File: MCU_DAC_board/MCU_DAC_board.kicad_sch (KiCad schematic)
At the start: 53 parts, among them J11 105-0752-001, J12 Conn_01x03_Pin, J5 54-00127, J6 105-0752-001, J7 Screw_Terminal_01x02, J8 Screw_Terminal_01x02, J9 Conn_02x20_Odd_Even, Q1 FZT953, U1 ADAU1966AWBSTZ

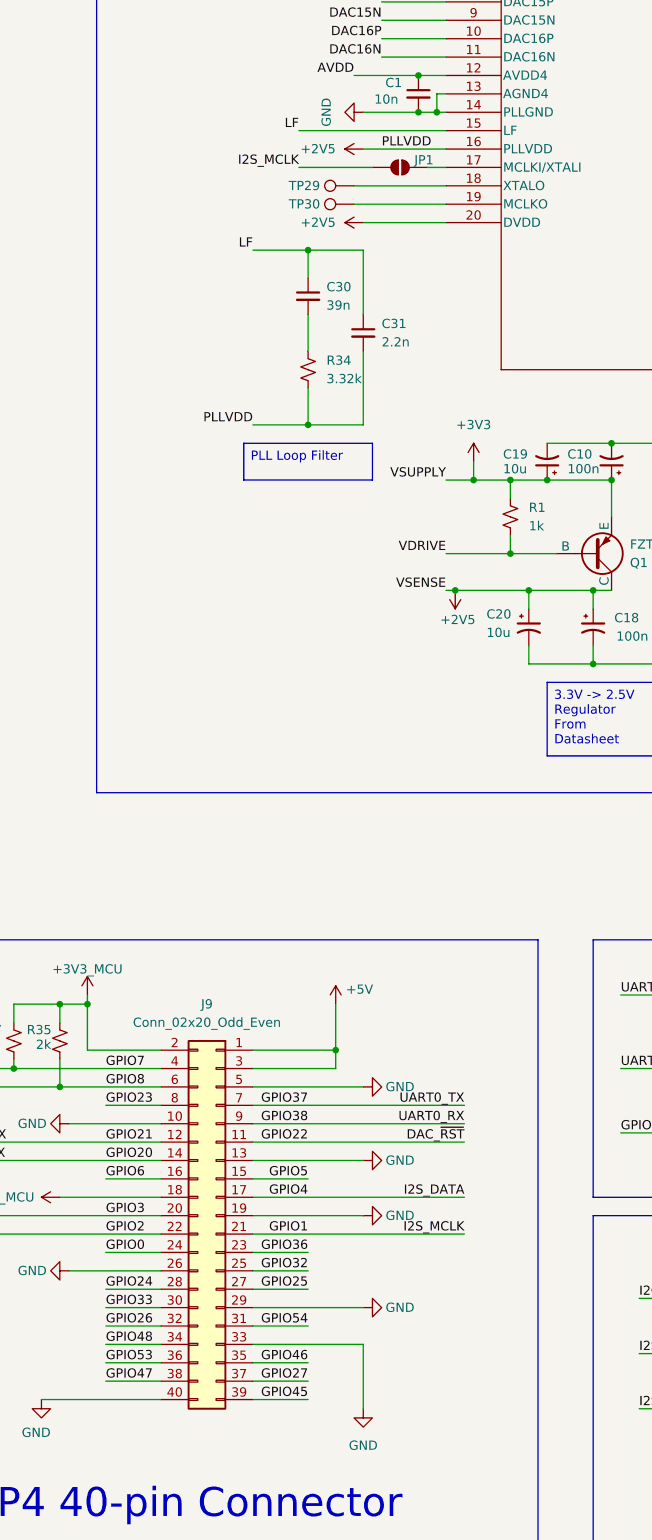
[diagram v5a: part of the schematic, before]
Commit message: Finished MCU to DAC signal routing
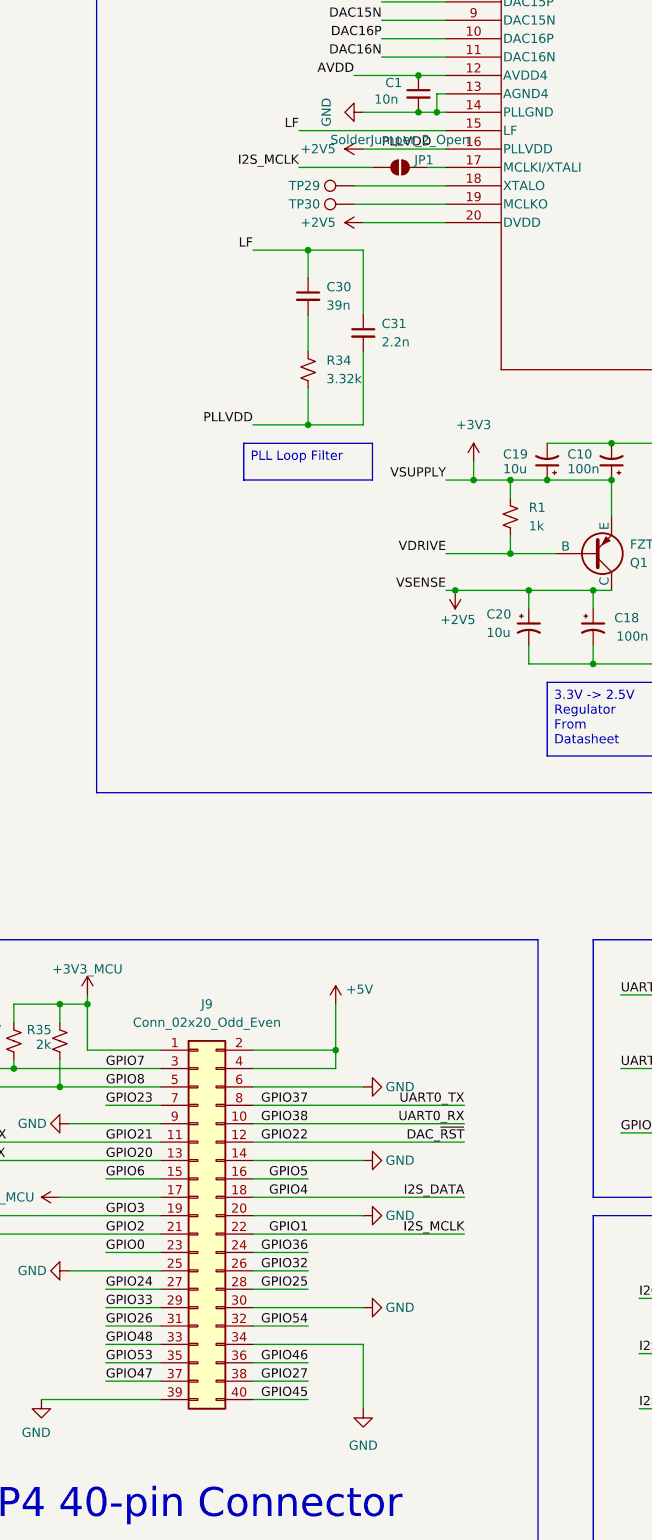
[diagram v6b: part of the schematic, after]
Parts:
- H1, H2, H3, H4: footprint (none) -> MountingHole:MountingHole_2.7mm_M2.5_DIN965_Pad_TopBottom
- JP1: footprint (none) -> Resistor_SMD:R_0201_0603Metric_Pad0.64x0.40mm_HandSolder
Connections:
- net +3V3_MCU: now also J9.1 (Pin_1), J9.17 (Pin_17); no longer J9.18 (Pin_18), J9.2 (Pin_2)
- net +5V: now also J9.2 (Pin_2), J9.4 (Pin_4); no longer J9.1 (Pin_1), J9.3 (Pin_3)
- net DAC_~{RST}: now also J9.12 (Pin_12); no longer J9.11 (Pin_11)
- net GND: now also J9.14 (Pin_14), J9.20 (Pin_20), J9.25 (Pin_25), J9.30 (Pin_30), J9.34 (Pin_34), J9.39 (Pin_39), J9.6 (Pin_6), J9.9 (Pin_9); no longer J9.10 (Pin_10), J9.13 (Pin_13), J9.19 (Pin_19), J9.26 (Pin_26), J9.29 (Pin_29), J9.33 (Pin_33), J9.40 (Pin_40), J9.5 (Pin_5)
- net GPIO0: now also J9.23 (Pin_23); no longer J9.24 (Pin_24)
- net GPIO1: now also J9.22 (Pin_22); no longer J9.21 (Pin_21)
- net GPIO2: now also J9.21 (Pin_21); no longer J9.22 (Pin_22)
- net GPIO20: now also J9.13 (Pin_13); no longer J9.14 (Pin_14)
- net GPIO21: now also J9.11 (Pin_11); no longer J9.12 (Pin_12)
- net GPIO23: now also J9.7 (Pin_7); no longer J9.8 (Pin_8)
- net GPIO24: now also J9.27 (Pin_27); no longer J9.28 (Pin_28)
- net GPIO25: now also J9.28 (Pin_28); no longer J9.27 (Pin_27)
- net GPIO26: now also J9.31 (Pin_31); no longer J9.32 (Pin_32)
- net GPIO27: now also J9.38 (Pin_38); no longer J9.37 (Pin_37)
- net GPIO3: now also J9.19 (Pin_19); no longer J9.20 (Pin_20)
- net GPIO32: now also J9.26 (Pin_26); no longer J9.25 (Pin_25)
- net GPIO33: now also J9.29 (Pin_29); no longer J9.30 (Pin_30)
- net GPIO36: now also J9.24 (Pin_24); no longer J9.23 (Pin_23)
- net GPIO37: now also J9.8 (Pin_8); no longer J9.7 (Pin_7)
- net GPIO38: now also J9.10 (Pin_10); no longer J9.9 (Pin_9)
- net GPIO4: now also J9.18 (Pin_18); no longer J9.17 (Pin_17)
- net GPIO45: now also J9.40 (Pin_40); no longer J9.39 (Pin_39)
- net GPIO46: now also J9.36 (Pin_36); no longer J9.35 (Pin_35)
- net GPIO47: now also J9.37 (Pin_37); no longer J9.38 (Pin_38)
- net GPIO48: now also J9.33 (Pin_33); no longer J9.34 (Pin_34)
- net GPIO5: now also J9.16 (Pin_16); no longer J9.15 (Pin_15)
- net GPIO53: now also J9.35 (Pin_35); no longer J9.36 (Pin_36)
- net GPIO54: now also J9.32 (Pin_32); no longer J9.31 (Pin_31)
- net GPIO6: now also J9.15 (Pin_15); no longer J9.16 (Pin_16)
- net GPIO7: now also J9.3 (Pin_3); no longer J9.4 (Pin_4)
- net GPIO8: now also J9.5 (Pin_5); no longer J9.6 (Pin_6)
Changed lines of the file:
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@@
 		)
 	)
-	(label "GPIO3"
-		(at 207.01 355.6 0)
-		(effects
-			(font
-				(size 1.27 1.27)
-			)
-			(justify left bottom)
-		)
-	)
 	(label "GPIO47"
 		(at 207.01 378.46 0)
@@
 		)
 	)
+	(label "GPIO3"
+		(at 207.01 355.6 0)
+		(effects
+			(font
+				(size 1.27 1.27)
+			)
+			(justify left bottom)
+		)
+	)
 	(label "AVDD"
 		(at 233.68 175.26 180)
@@
 			)
 		)
-		(property "Footprint" ""
+		(property "Footprint" "MountingHole:MountingHole_2.7mm_M2.5_DIN965_Pad_TopBottom"
 			(at 165.1 107.95 0)
 			(effects
@@
 			)
 		)
-		(property "Footprint" ""
+		(property "Footprint" "MountingHole:MountingHole_2.7mm_M2.5_DIN965_Pad_TopBottom"
 			(at 135.89 107.95 0)
 			(effects
@@
 			)
 		)
-		(property "Footprint" ""
+		(property "Footprint" "MountingHole:MountingHole_2.7mm_M2.5_DIN965_Pad_TopBottom"
 			(at 135.89 92.71 0)
 			(effects
@@
 			)
 		)
-		(property "Footprint" ""
+		(property "Footprint" "MountingHole:MountingHole_2.7mm_M2.5_DIN965_Pad_TopBottom"
 			(at 165.1 92.71 0)
 			(effects
@@
 					(size 1.27 1.27)
 				)
-				(hide yes)
 			)
 		)
-		(property "Footprint" ""
+		(property "Footprint" "Resistor_SMD:R_0201_0603Metric_Pad0.64x0.40mm_HandSolder"
 			(at 247.65 210.82 0)
 			(effects
@@
 	(symbol
 		(lib_id "Connector_Generic:Conn_02x20_Odd_Even")
-		(at 222.25 355.6 0)
-		(mirror y)
+		(at 219.71 355.6 0)
 		(unit 1)
 		(exclude_from_sim no)
@@
 		)
 		(property "Footprint" "Connector_PinSocket_2.54mm:PinSocket_2x20_P2.54mm_Vertical_SMD"
-			(at 222.25 355.6 0)
+			(at 219.71 355.6 0)
 			(effects
 				(font
@@
 		)
 		(property "Datasheet" "~"
-			(at 222.25 355.6 0)
+			(at 219.71 355.6 0)
 			(effects
 				(font
@@
 		)
 		(property "Description" "Generic connector, double row, 02x20, odd/even pin numbering scheme (row 1 odd numbers, row 2 even numbers), script generated (kicad-library-utils/schlib/autogen/connector/)"
-			(at 222.25 355.6 0)
+			(at 219.71 355.6 0)
 			(effects
 				(font

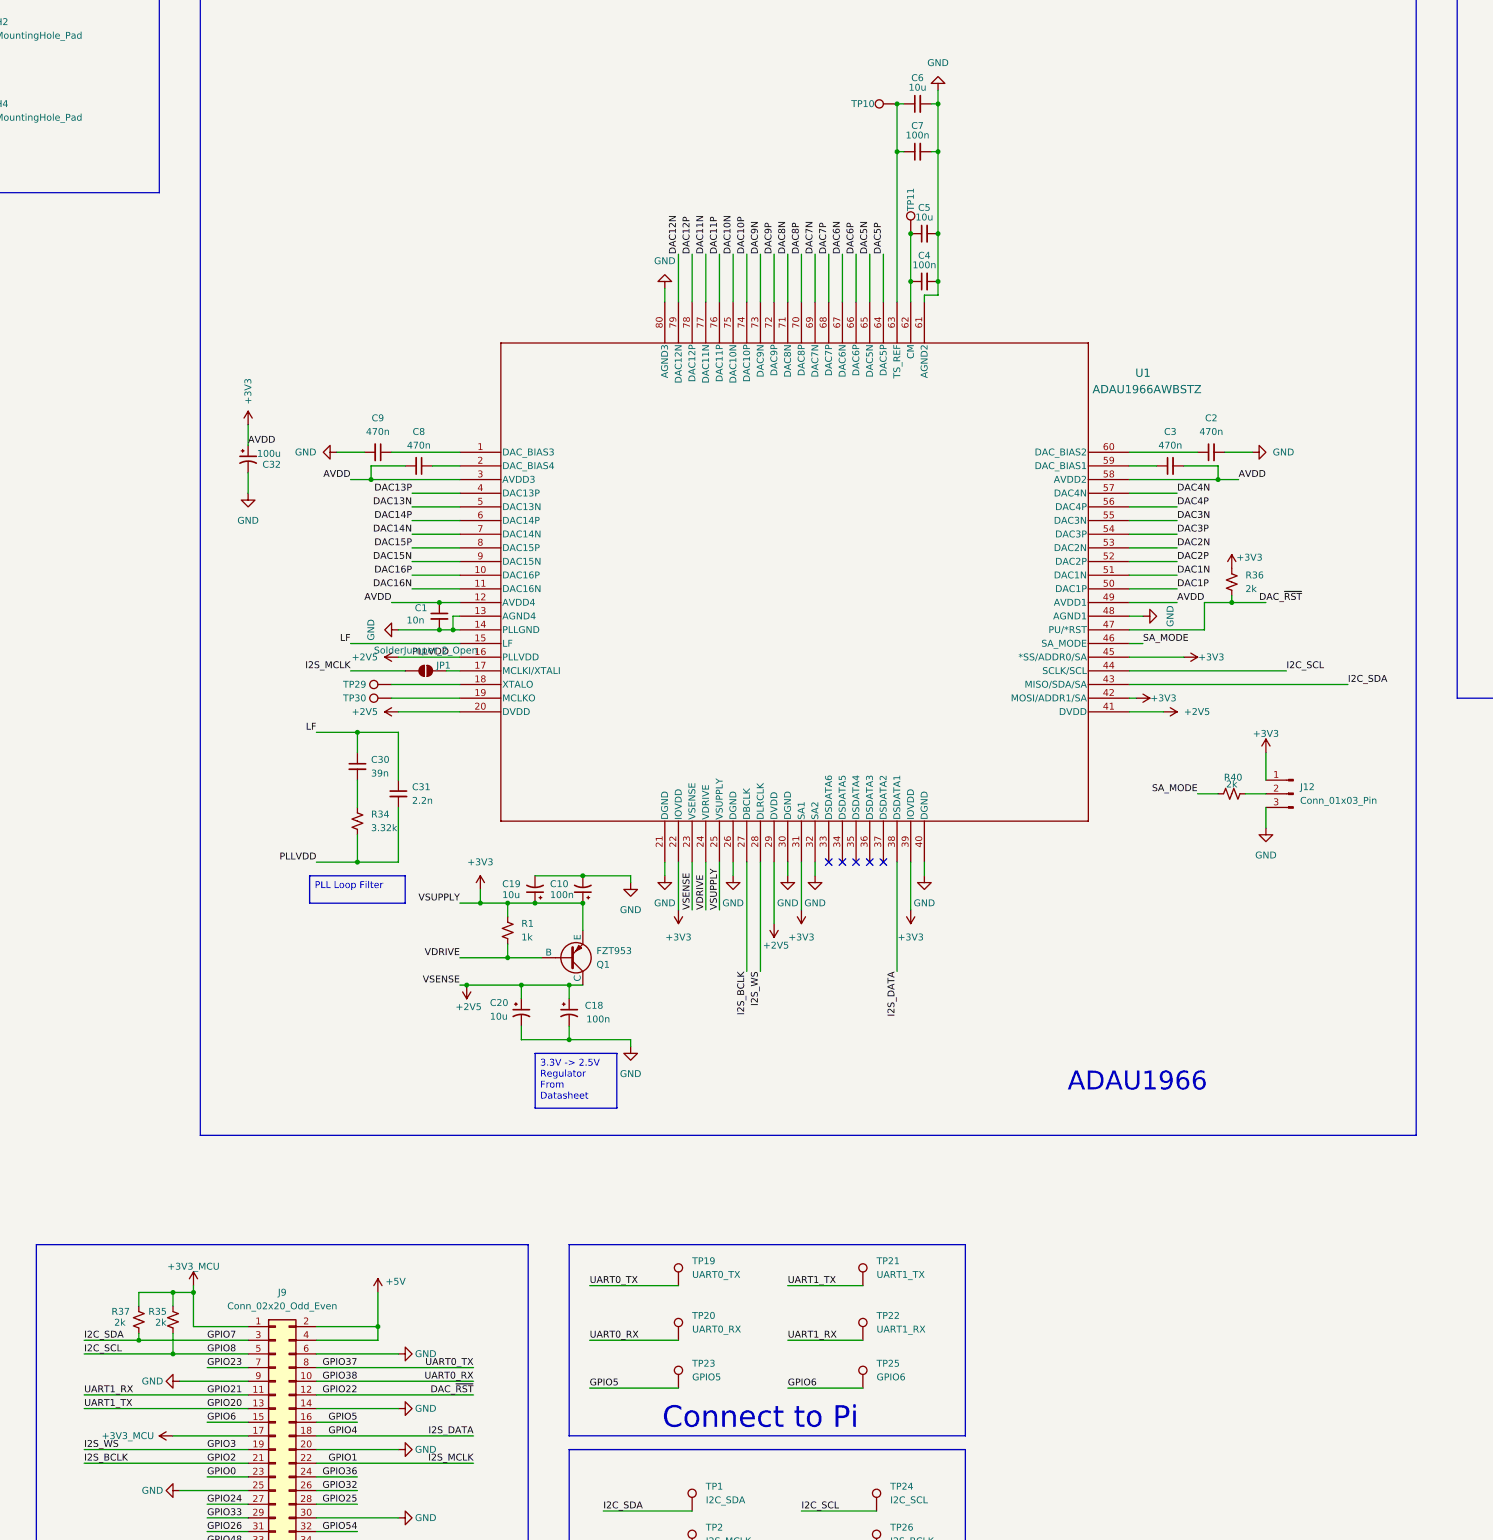
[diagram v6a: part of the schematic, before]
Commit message: DAC board layout (mostly) done
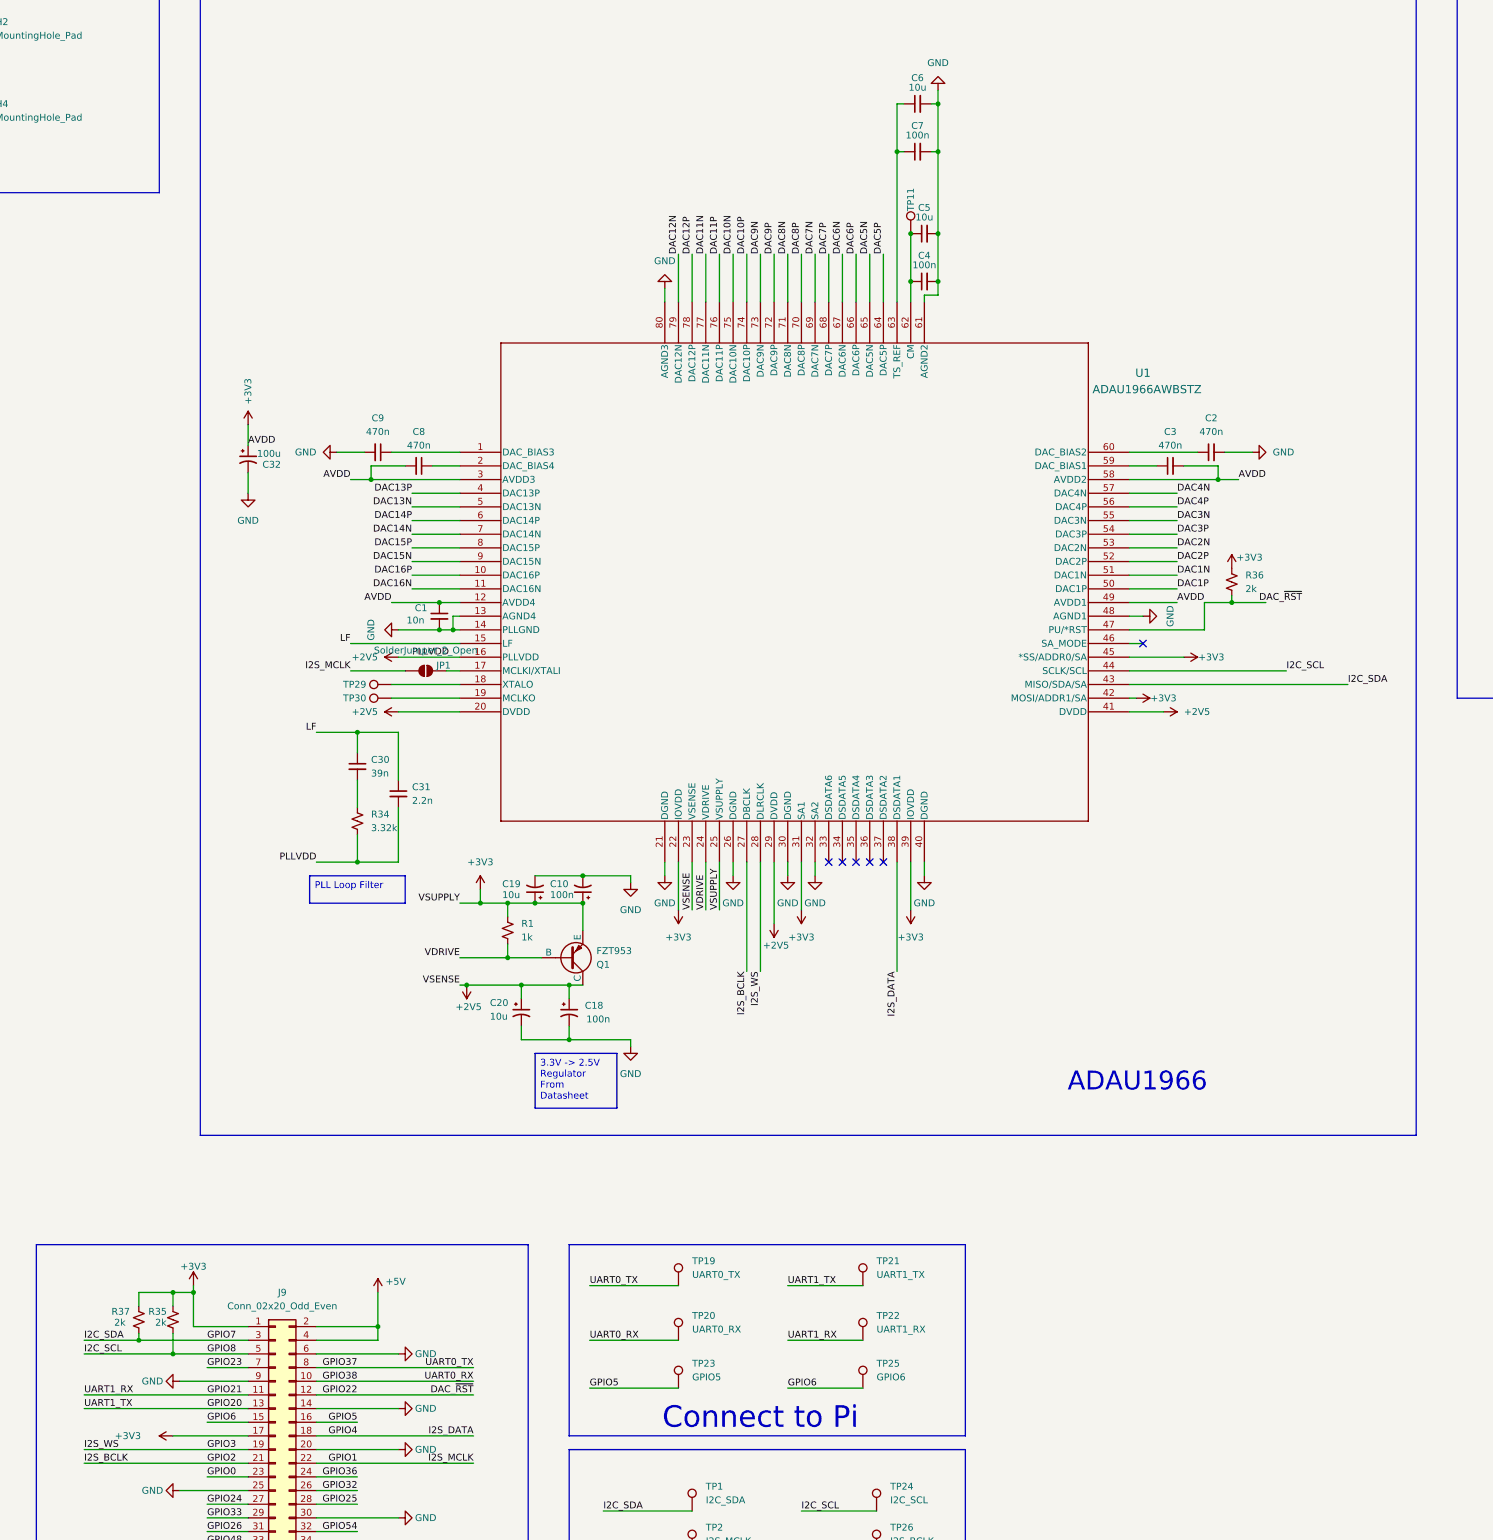
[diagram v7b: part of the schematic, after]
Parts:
- removed J12: Conn_01x03_Pin, Connector_PinHeader_2.54mm:PinHeader_1x03_P2.54mm_Vertical, symbol Connector:Conn_01x03_Pin
- removed R40: 2k, Resistor_SMD:R_0805_2012Metric_Pad1.20x1.40mm_HandSolder, symbol Device:R_Small_US
- removed TP10: TS_REF, project_lib:TP_1.8x1mm, symbol Connector:TestPoint
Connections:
- net +3V3_MCU is gone; now on net +3V3: J9.1 (Pin_1), J9.17 (Pin_17), R35.1, R37.1
- net SA_MODE: no longer names the net of U1.46 (SA_MODE)
- no-connect marks 5 -> 6
